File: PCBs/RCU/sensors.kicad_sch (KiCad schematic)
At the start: 11 parts, among them U501 LSM6DS3

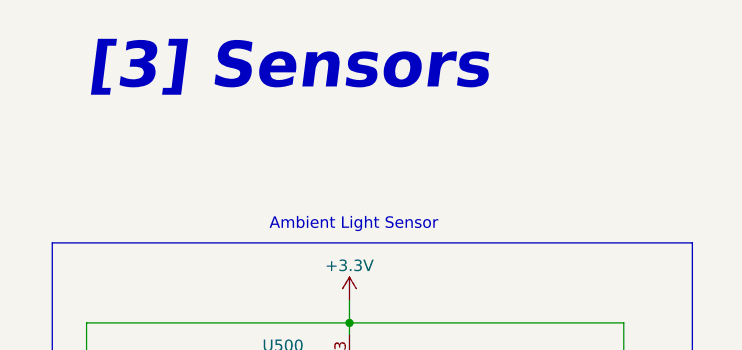
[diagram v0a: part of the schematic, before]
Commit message: Changed internal numbering of Sensors schematic from 3 to 5
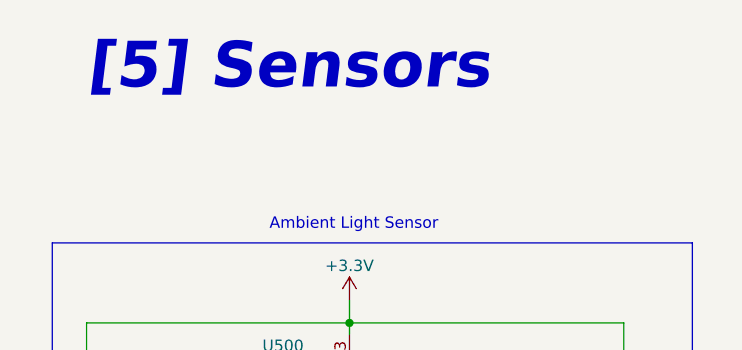
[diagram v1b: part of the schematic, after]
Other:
- note added: "[5] Sensors"
- note removed: "[3] Sensors"
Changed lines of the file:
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@@
     (effects (font (size 1.27 1.27)) (justify left bottom))
   )
-  (text "[3] Sensors" (at 21.59 27.94 0)
+  (text "[5] Sensors" (at 21.59 27.94 0)
     (effects (font (size 5.08 5.08) (thickness 1.016) bold italic) (justify left bottom))
   )

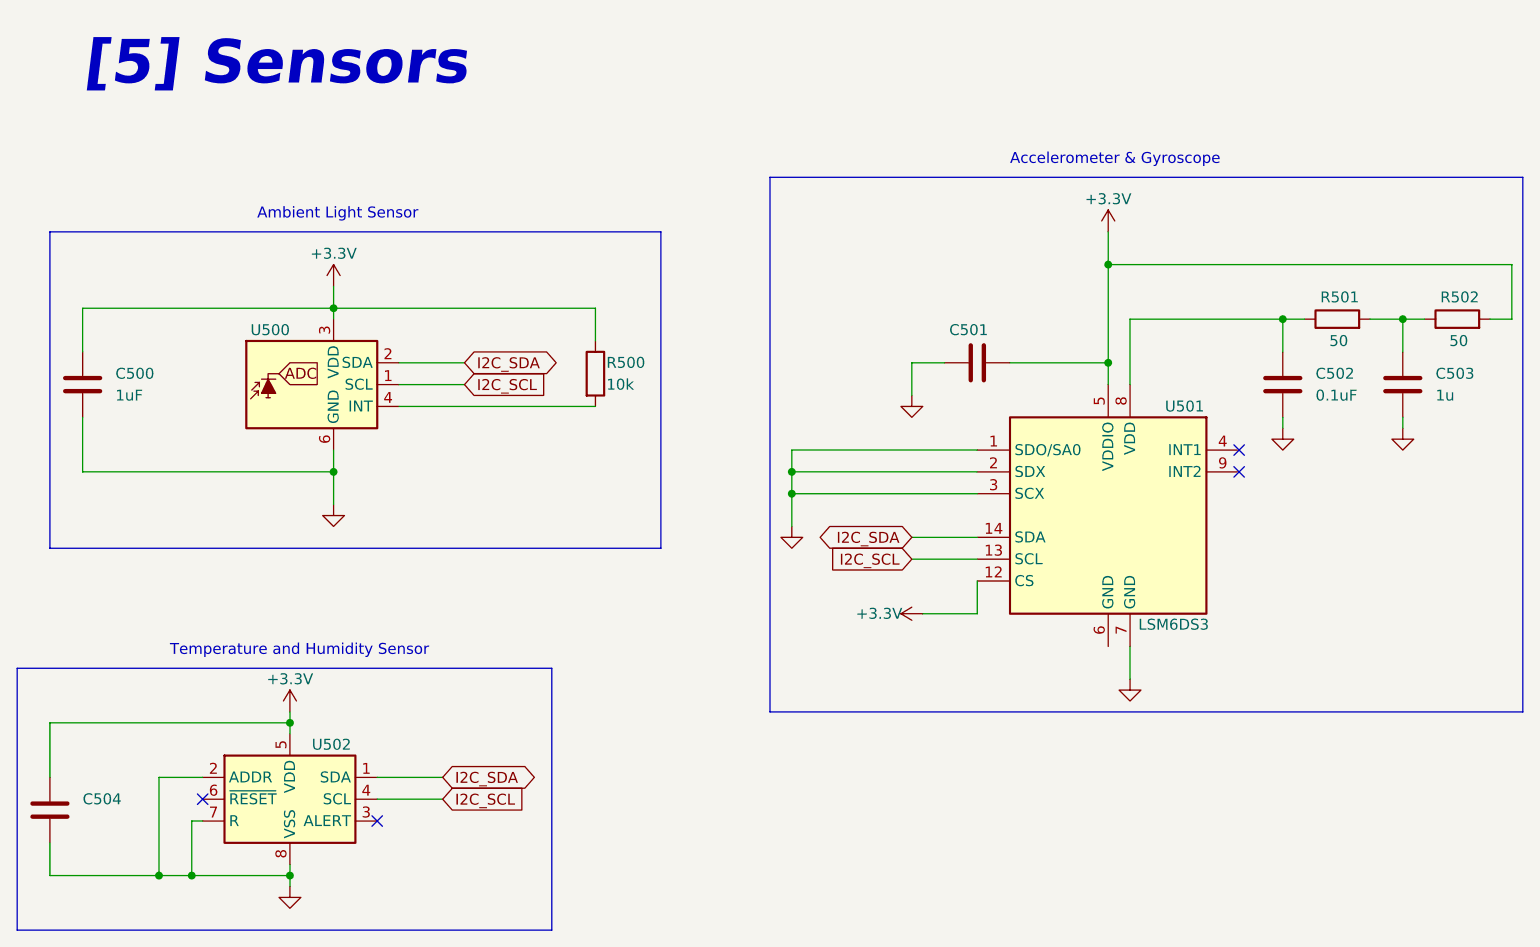
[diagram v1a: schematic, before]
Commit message: The shared SWCLK/BOOT0 pin has an internal pull-down resistor, and in the case where SWCLK is shared and are programming with SWD, just need NRST conncted to the STLink-V2 module
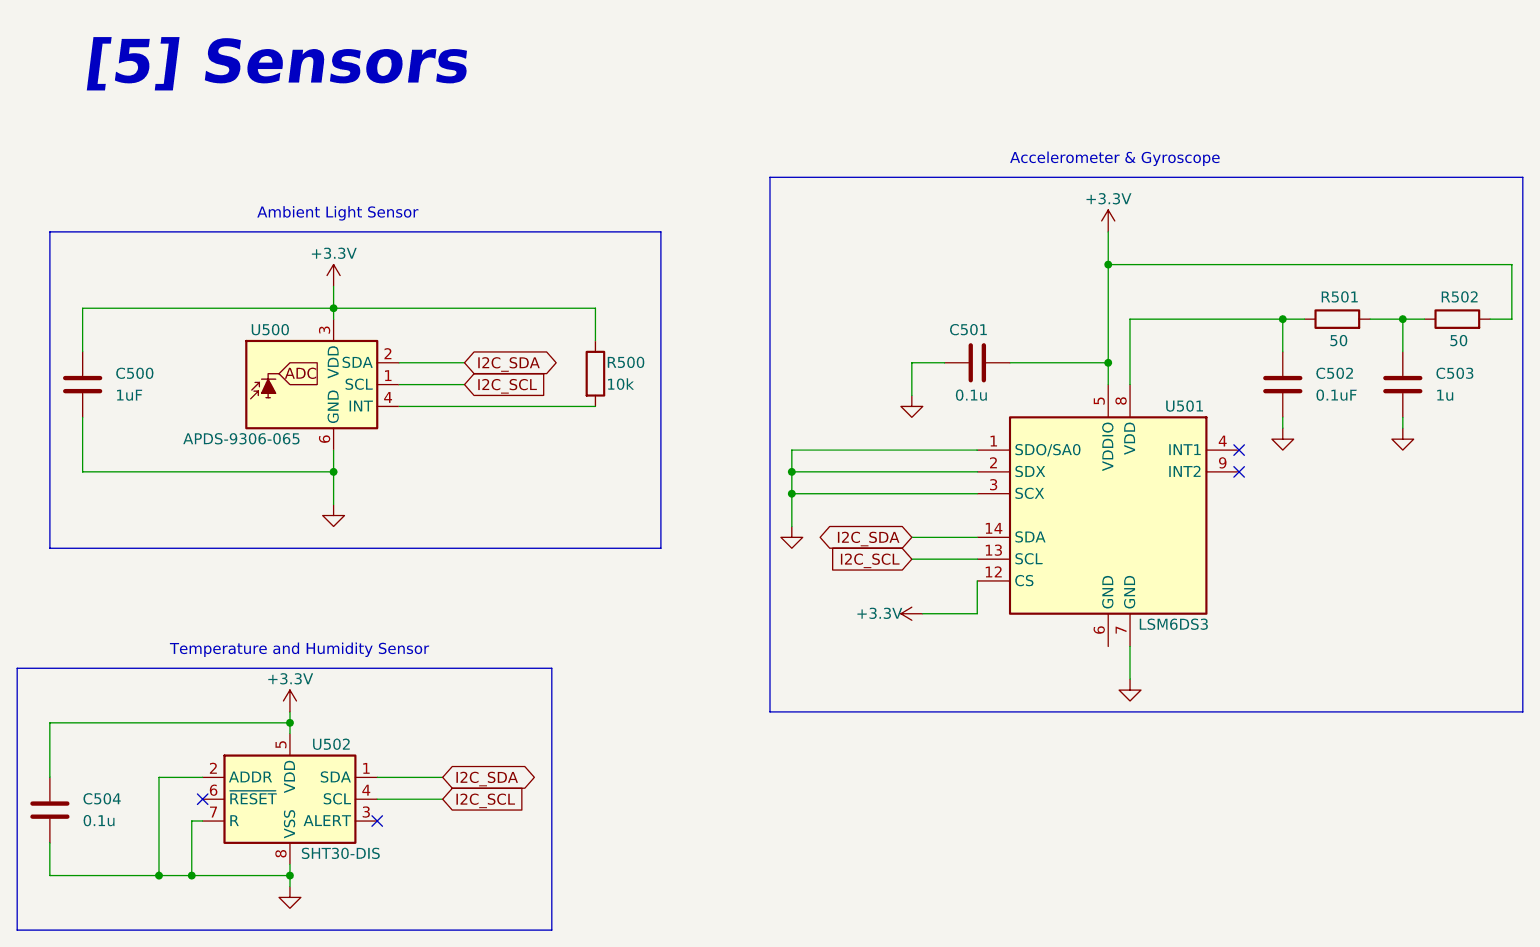
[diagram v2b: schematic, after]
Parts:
- C501, C504: value (none) -> 0.1u
- U500: value (none) -> APDS-9306-065; footprint (none) -> OptoDevice:Broadcom_DFN-6_2x2mm_P0.65mm
- U502: value (none) -> SHT30-DIS; footprint (none) -> Sensor_Humidity:Sensirion_DFN-8-1EP_2.5x2.5mm_P0.5mm_EP1.1x1.7mm
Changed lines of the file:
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@@
       (effects (font (size 1.27 1.27)) (justify left))
     )
-    (property "Value" "" (id 1) (at 46.99 116.84 0)
-      (effects (font (size 1.27 1.27)) (justify left))
-    )
-    (property "Footprint" "" (id 2) (at 45.72 109.22 0)
+    (property "Value" "SHT30-DIS" (id 1) (at 46.99 116.84 0)
+      (effects (font (size 1.27 1.27)) (justify left))
+    )
+    (property "Footprint" "Sensor_Humidity:Sensirion_DFN-8-1EP_2.5x2.5mm_P0.5mm_EP1.1x1.7mm" (id 2) (at 45.72 109.22 0)
       (effects (font (size 1.27 1.27)) hide)
     )
@@
       (effects (font (size 1.27 1.27)) (justify right))
     )
-    (property "Value" "" (id 1) (at 46.99 68.58 0)
-      (effects (font (size 1.27 1.27)) (justify right))
-    )
-    (property "Footprint" "" (id 2) (at 48.26 74.93 0)
+    (property "Value" "APDS-9306-065" (id 1) (at 46.99 68.58 0)
+      (effects (font (size 1.27 1.27)) (justify right))
+    )
+    (property "Footprint" "OptoDevice:Broadcom_DFN-6_2x2mm_P0.65mm" (id 2) (at 48.26 74.93 0)
       (effects (font (size 1.27 1.27)) hide)
     )
@@
       (effects (font (size 1.27 1.27)) (justify left))
     )
-    (property "Value" "" (id 1) (at 21.59 113.0299 0)
+    (property "Value" "0.1u" (id 1) (at 21.59 113.0299 0)
       (effects (font (size 1.27 1.27)) (justify left))
     )
@@
       (effects (font (size 1.27 1.27)) (justify left))
     )
-    (property "Value" "" (id 1) (at 127 63.5 90)
-      (effects (font (size 1.27 1.27)) (justify left))
-    )
+    (property "Value" "0.1u" (id 1) (at 127 63.5 90)
+      (effects (font (size 1.27 1.27)) (justify left))
+    )

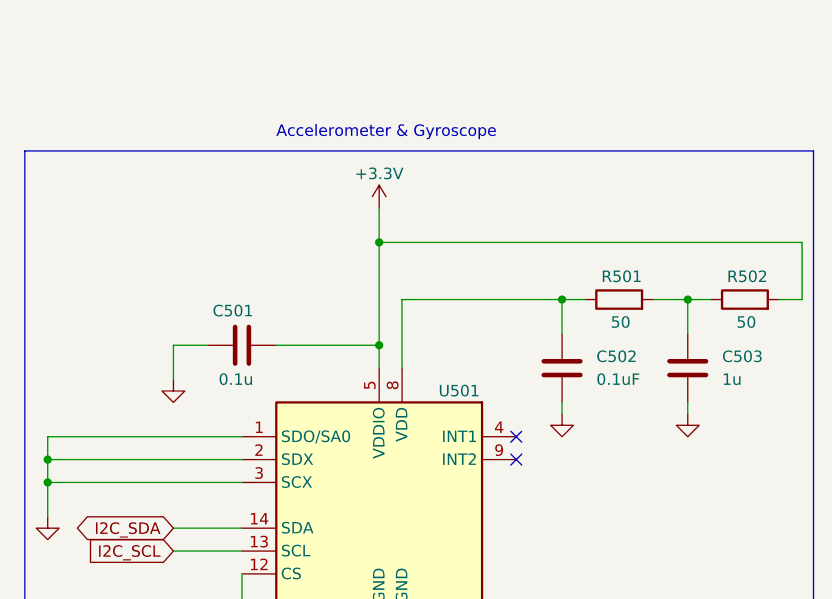
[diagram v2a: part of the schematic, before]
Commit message: Delete low pass filter for VDD for LSM6DS3 in sensors module, datasheet only recommend 100nF cap
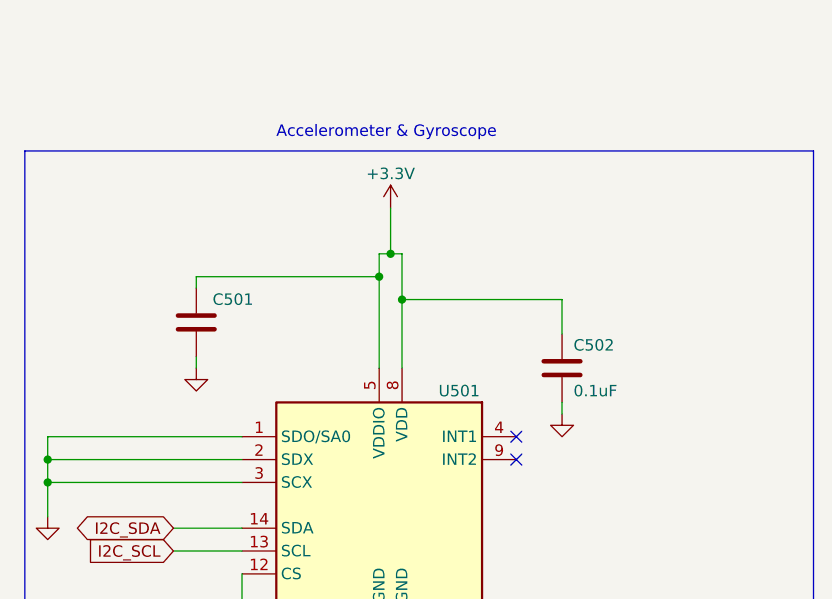
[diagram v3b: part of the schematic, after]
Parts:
- removed C503: 1u, symbol Device:C
- removed R501, R502: 50, symbol Device:R
- C501: value 0.1u -> (none)
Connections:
- net +3V3: now also C502.2, U501.8 (VDD)
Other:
- moved on the sheet: C501

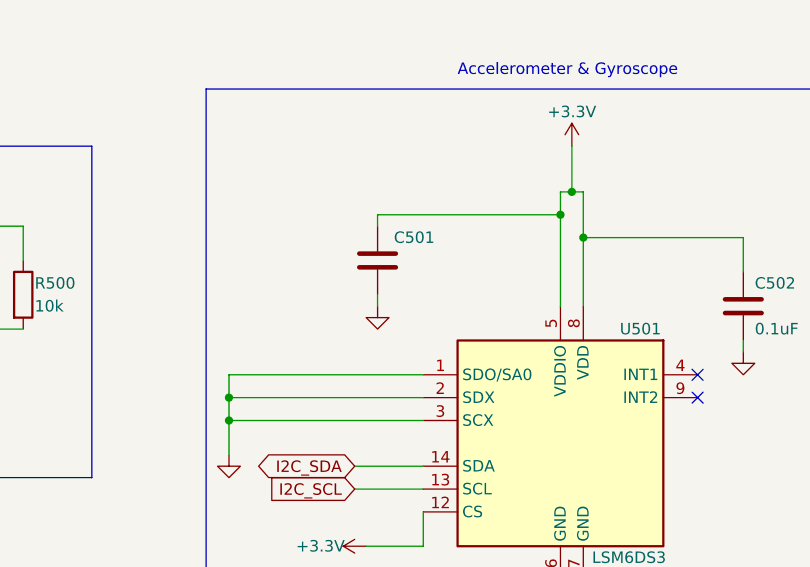
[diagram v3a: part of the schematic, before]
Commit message: Updated ADC schematic to match application note in ADC and op-amp data sheets
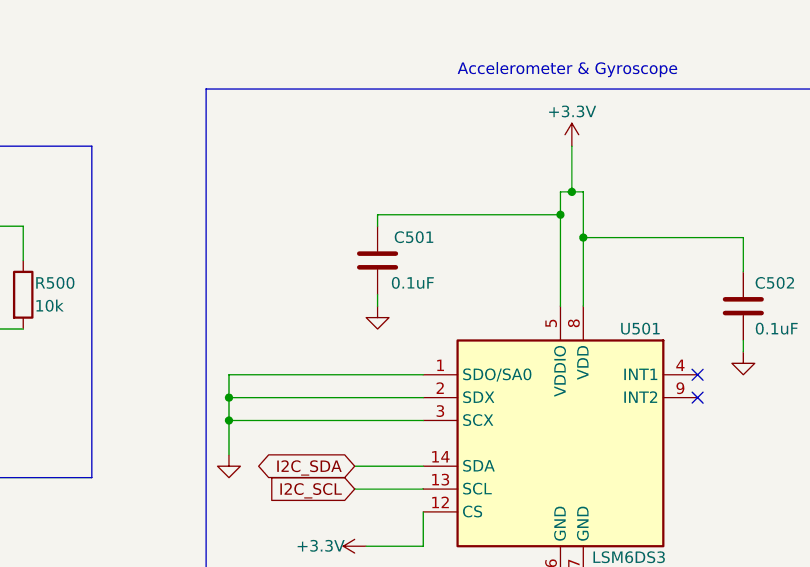
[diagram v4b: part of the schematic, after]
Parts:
- C501: value (none) -> 0.1uF
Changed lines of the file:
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@@
       (effects (font (size 1.27 1.27)) (justify left))
     )
-    (property "Value" "" (id 1) (at 127 59.69 0)
+    (property "Value" "0.1uF" (id 1) (at 127 59.69 0)
       (effects (font (size 1.27 1.27)) (justify left))
     )
